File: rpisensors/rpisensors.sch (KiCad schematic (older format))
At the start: 8 parts, among them J1 Conn_02x20_Odd_Even, J2 Conn_01x08_Male, J3 Conn_01x08_Male, J4 Conn_01x08_Male, J5 Conn_01x08_Male, J6 Conn_01x08_Male, J7 Conn_01x08_Male

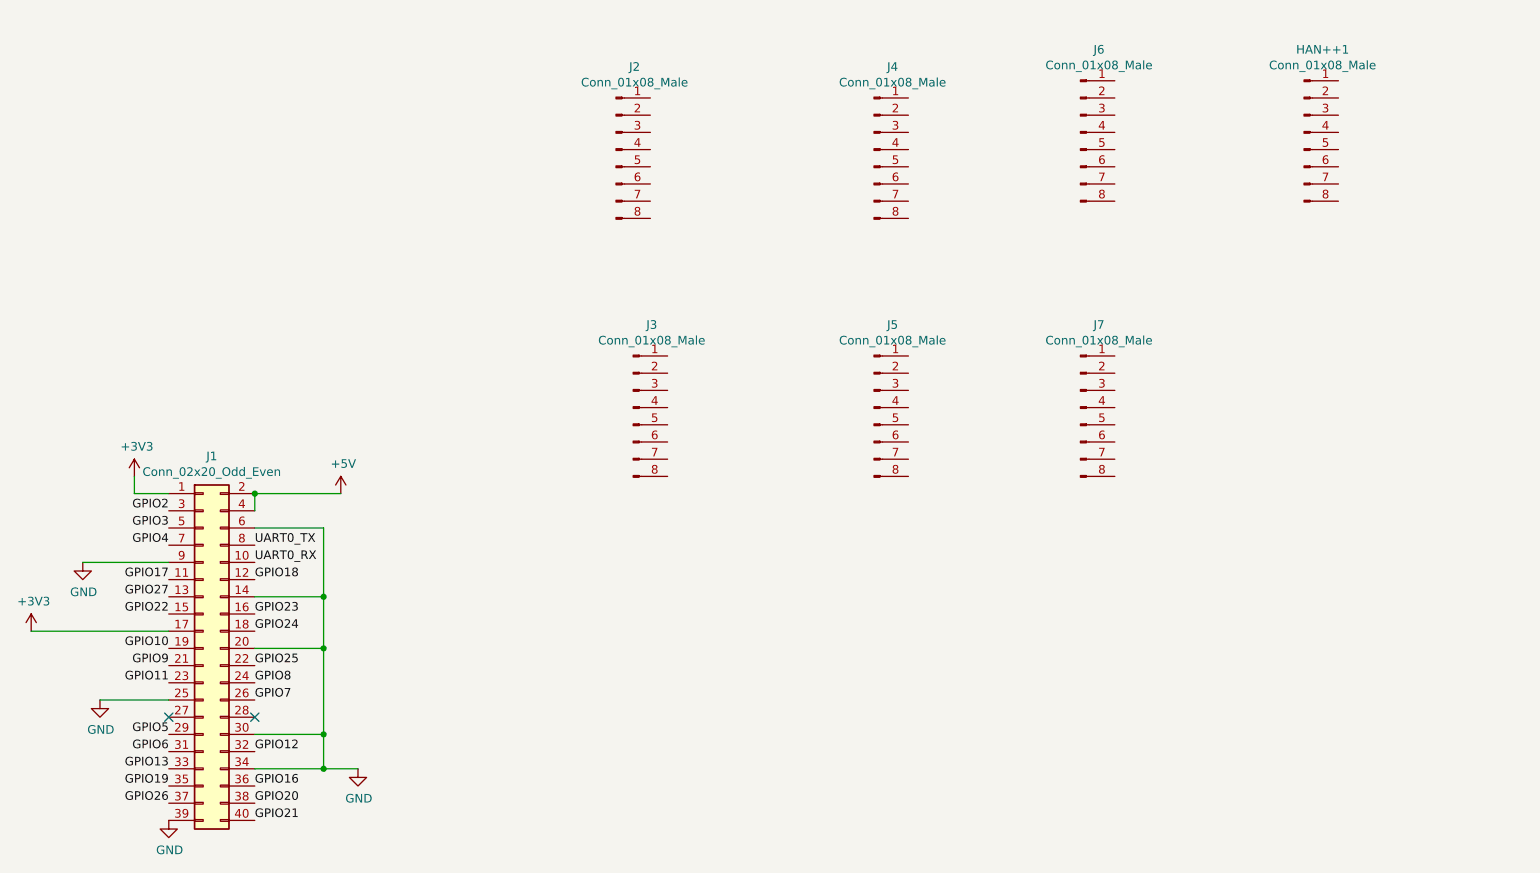
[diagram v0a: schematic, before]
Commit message: Added wiring. Lacks silkscreen and final touch
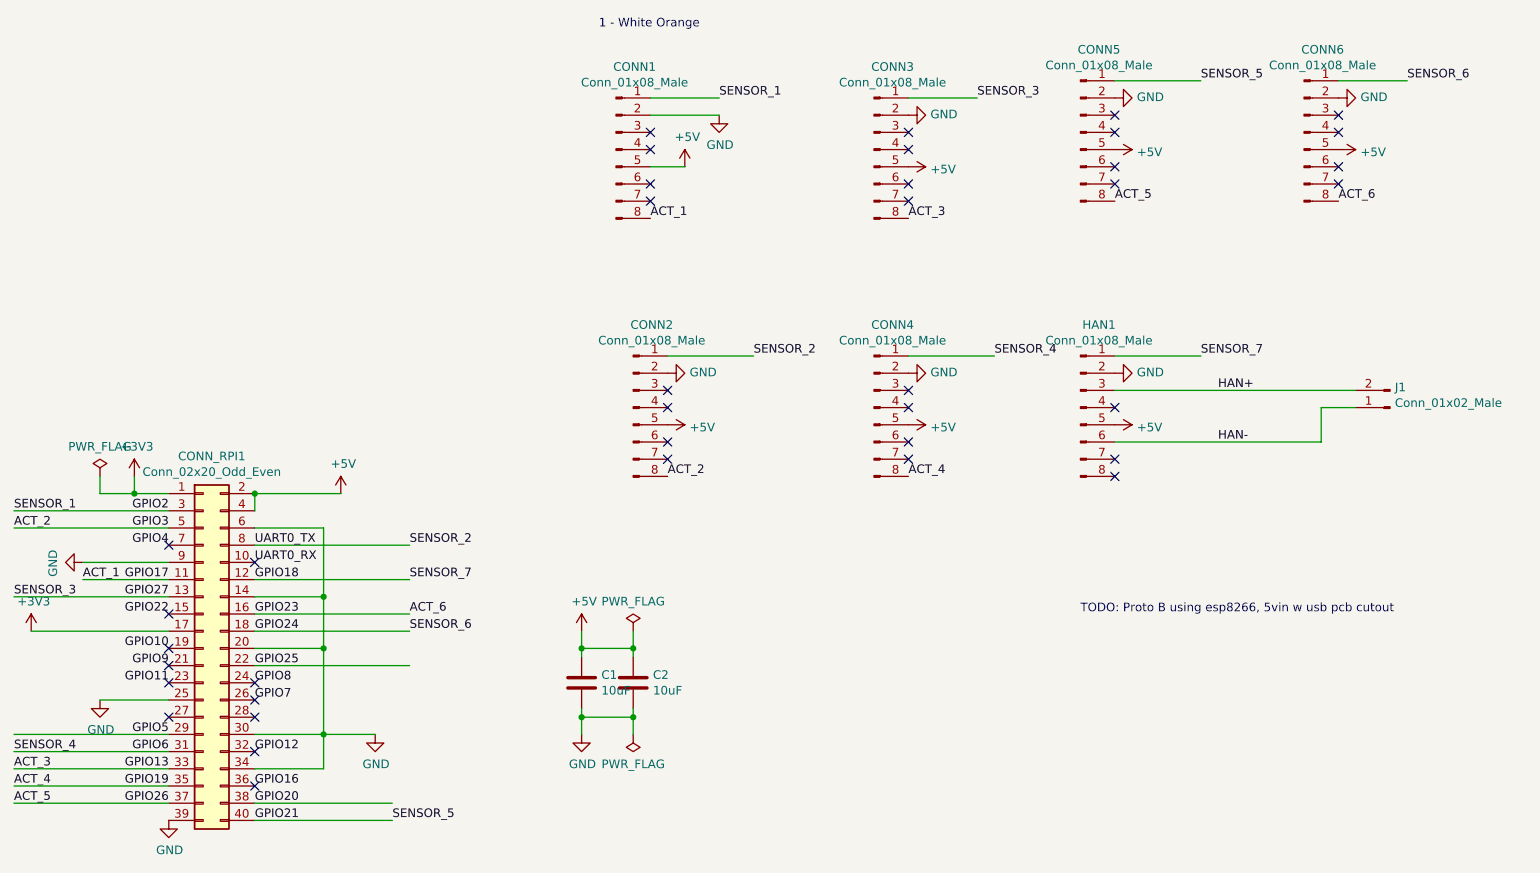
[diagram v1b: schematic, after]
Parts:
- added C1, C2: 10uF, Capacitors_THT:CP_Radial_D5.0mm_P2.50mm, symbol Device:C
- added J1: Conn_01x02_Male, Connectors:PINHEAD1-2, symbol Connector:Conn_01x02_Male
- renumbered J2 to CONN1, J3 to CONN2, J4 to CONN3, J5 to CONN4, J6 to CONN5, HAN++1 to CONN6, J1 to CONN_RPI1, J7 to HAN1
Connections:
- net labels added: ACT_1, ACT_2, ACT_3, ACT_4, ACT_5, ACT_6, HAN+, HAN-, SENSOR_1, SENSOR_2, SENSOR_3, SENSOR_4, SENSOR_5, SENSOR_6, SENSOR_7
- wire segments 17 -> 58
- no-connect marks 2 -> 39
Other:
- note added: "1 - White Orange"
- note added: "TODO: Proto B using esp8266, 5vin w usb pcb cutout"
